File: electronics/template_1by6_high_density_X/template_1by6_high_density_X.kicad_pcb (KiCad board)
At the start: 2 copper layers, 19 x 49 mm, 16 parts, among them J1 1, J10 10, J11 11, J12 12, J13 13, J14 14, J2 2, J3 3, J4 4, J5 5, J6 6, J7 7, J8 8, J9 9

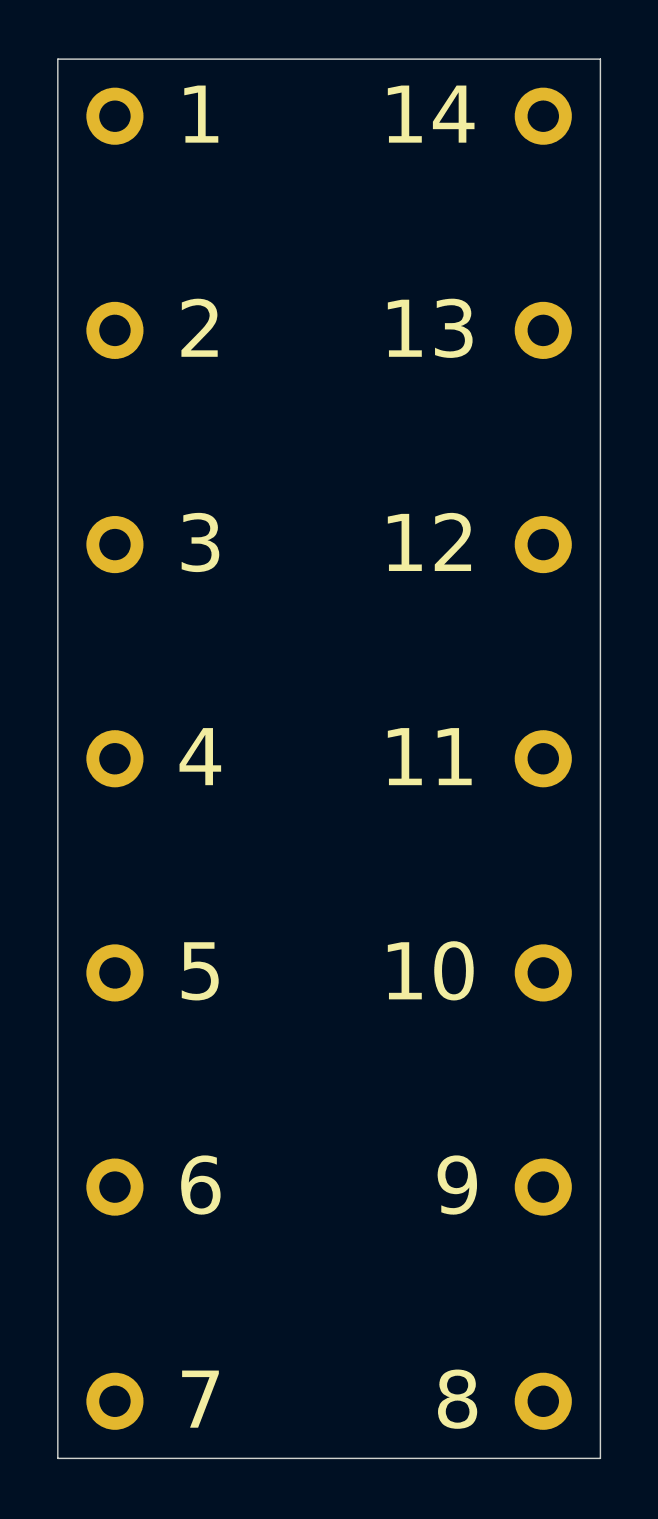
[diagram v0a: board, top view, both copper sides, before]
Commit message: completed high density X templates, updated versionnumbers of high density XN templates
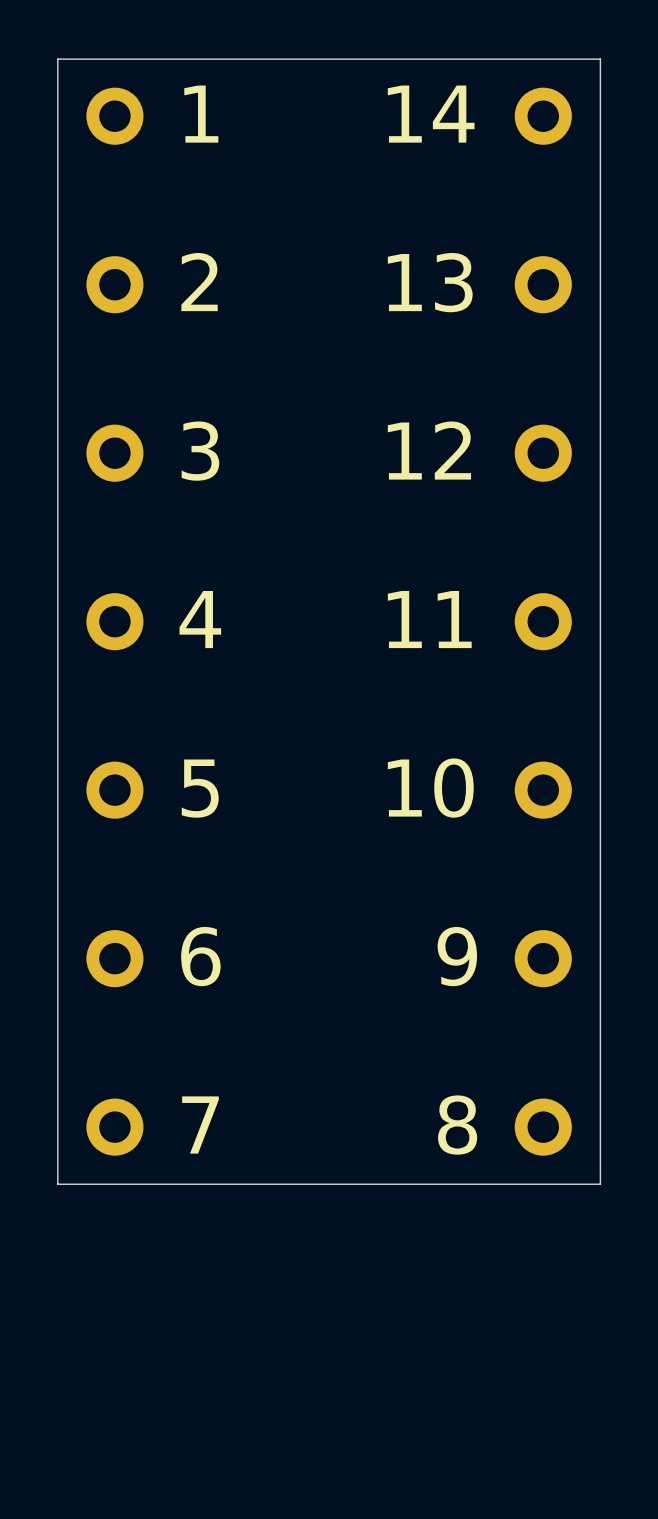
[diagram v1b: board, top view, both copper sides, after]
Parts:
- moved J7 9.60 mm to (142.5, 97.9)
- moved J8 9.60 mm to (157.5, 97.9)
- moved J6 8.00 mm to (142.5, 92.0)
- moved J9 8.00 mm to (157.5, 92.0)
- moved J10 6.40 mm to (157.5, 86.1)
- moved J5 6.40 mm to (142.5, 86.1)
- moved J11 4.80 mm to (157.5, 80.2)
- moved J4 4.80 mm to (142.5, 80.2)
- moved J12 3.20 mm to (157.5, 74.3)
- moved J3 3.20 mm to (142.5, 74.3)
- moved N1 2.50 mm to (150.9, 82.7)
- moved N2 2.50 mm to (150.0, 79.0)
- moved J13 1.60 mm to (157.5, 68.4)
- moved J2 1.60 mm to (142.5, 68.4)
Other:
- board size 19 x 49 mm -> 19 x 39.4 mm
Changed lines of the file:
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@@
   )
   (footprint "mill-max:PC_pin_nail_head_6092" locked (layer "F.Cu")
-    (at 142.5 70)
+    (at 142.5 68.4)
     (property "Sheetfile" "template_1by6.kicad_sch")
     (property "Sheetname" "")
@@
   )
   (footprint "mill-max:PC_pin_nail_head_6092" locked (layer "F.Cu")
-    (at 142.5 77.5)
+    (at 142.5 74.3)
     (property "Sheetfile" "template_1by6.kicad_sch")
     (property "Sheetname" "")
@@
   )
   (footprint "mill-max:PC_pin_nail_head_6092" locked (layer "F.Cu")
-    (at 142.5 92.5 180)
+    (at 142.5 86.1 180)
     (property "Sheetfile" "template_1by6.kicad_sch")
     (property "Sheetname" "")
@@
   )
   (footprint "mill-max:PC_pin_nail_head_6092" locked (layer "F.Cu")
-    (at 142.5 100 180)
+    (at 142.5 92 180)
     (property "Sheetfile" "template_1by6.kicad_sch")
     (property "Sheetname" "")
@@
   )
   (footprint "mill-max:PC_pin_nail_head_6092" locked (layer "F.Cu")
-    (at 142.5 85 180)
+    (at 142.5 80.2 180)
     (property "Sheetfile" "template_1by6.kicad_sch")
     (property "Sheetname" "")
@@
   )
   (footprint "mill-max:PC_pin_nail_head_6092" locked (layer "F.Cu")
-    (at 157.5 85)
+    (at 157.5 80.2)
     (property "Sheetfile" "template_1by6.kicad_sch")
     (property "Sheetname" "")
@@
   )
   (footprint "mill-max:PC_pin_nail_head_6092" locked (layer "F.Cu")
-    (at 157.5 107.5)
+    (at 157.5 97.9)
     (property "Sheetfile" "template_1by6.kicad_sch")
     (property "Sheetname" "")
@@
   )
   (footprint "mill-max:PC_pin_nail_head_6092" locked (layer "F.Cu")
-    (at 157.5 92.5)
+    (at 157.5 86.1)
     (property "Sheetfile" "template_1by6.kicad_sch")
     (property "Sheetname" "")
@@
   )
   (footprint "mill-max:PC_pin_nail_head_6092" locked (layer "F.Cu")
-    (at 157.5 70)
+    (at 157.5 68.4)
     (property "Sheetfile" "template_1by6.kicad_sch")
     (property "Sheetname" "")
@@
   )
   (footprint "mill-max:PC_pin_nail_head_6092" locked (layer "F.Cu")
-    (at 142.5 107.5)
+    (at 142.5 97.9)
     (property "Sheetfile" "template_1by6.kicad_sch")
     (property "Sheetname" "")
@@
   )
   (footprint "mill-max:PC_pin_nail_head_6092" locked (layer "F.Cu")
-    (at 157.5 100)
+    (at 157.5 92)
     (property "Sheetfile" "template_1by6.kicad_sch")
     (property "Sheetname" "")
@@
   )
   (footprint "mill-max:PC_pin_nail_head_6092" locked (layer "F.Cu")
-    (at 157.5 77.5)
+    (at 157.5 74.3)
     (property "Sheetfile" "template_1by6.kicad_sch")
     (property "Sheetname" "")
@@
   )
   (footprint "Symbol:OSHW-Symbol_6.7x6mm_SilkScreen" (layer "B.Cu")
-    (at 150 76.5 180)
+    (at 150 79 180)
     (descr "Open Source Hardware Symbol")
     (tags "Logo Symbol OSHW")
@@
   )
   (footprint "SquantorLabels:Label_Generic" (layer "B.Cu")
-    (at 150.9 80.2 180)
+    (at 150.9 82.7 180)
     (descr "Label for general purpose use")
     (tags "Label")
@@
       (stroke (width 0.15) (type solid)) (layer "B.SilkS"))
   )
-  (gr_line (start 140.5 109.5) (end 159.5 109.5)
+  (gr_line (start 140.5 99.9) (end 159.5 99.9)
     (stroke (width 0.05) (type solid)) (layer "Edge.Cuts"))
-  (gr_line (start 159.5 60.5) (end 159.5 109.5)
+  (gr_line (start 159.5 60.5) (end 159.5 99.9)
     (stroke (width 0.05) (type solid)) (layer "Edge.Cuts"))
   (gr_line (start 159.5 60.5) (end 140.5 60.5)
     (stroke (width 0.05) (type solid)) (layer "Edge.Cuts"))
-  (gr_line (start 140.5 109.5) (end 140.5 60.5)
+  (gr_line (start 140.5 99.9) (end 140.5 60.5)
     (stroke (width 0.05) (type solid)) (layer "Edge.Cuts"))
 )
